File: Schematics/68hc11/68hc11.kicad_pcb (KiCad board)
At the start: 2 copper layers, 14 parts, among them J1 DB9_Female_MountingHoles, U1 MC68HC11A1CC-PLLC, U2 MC68B21, U3 74HC373, U4 74HC245, U6 27C64, U7 27C64, U8 HM62256BLP, U9 MAX232

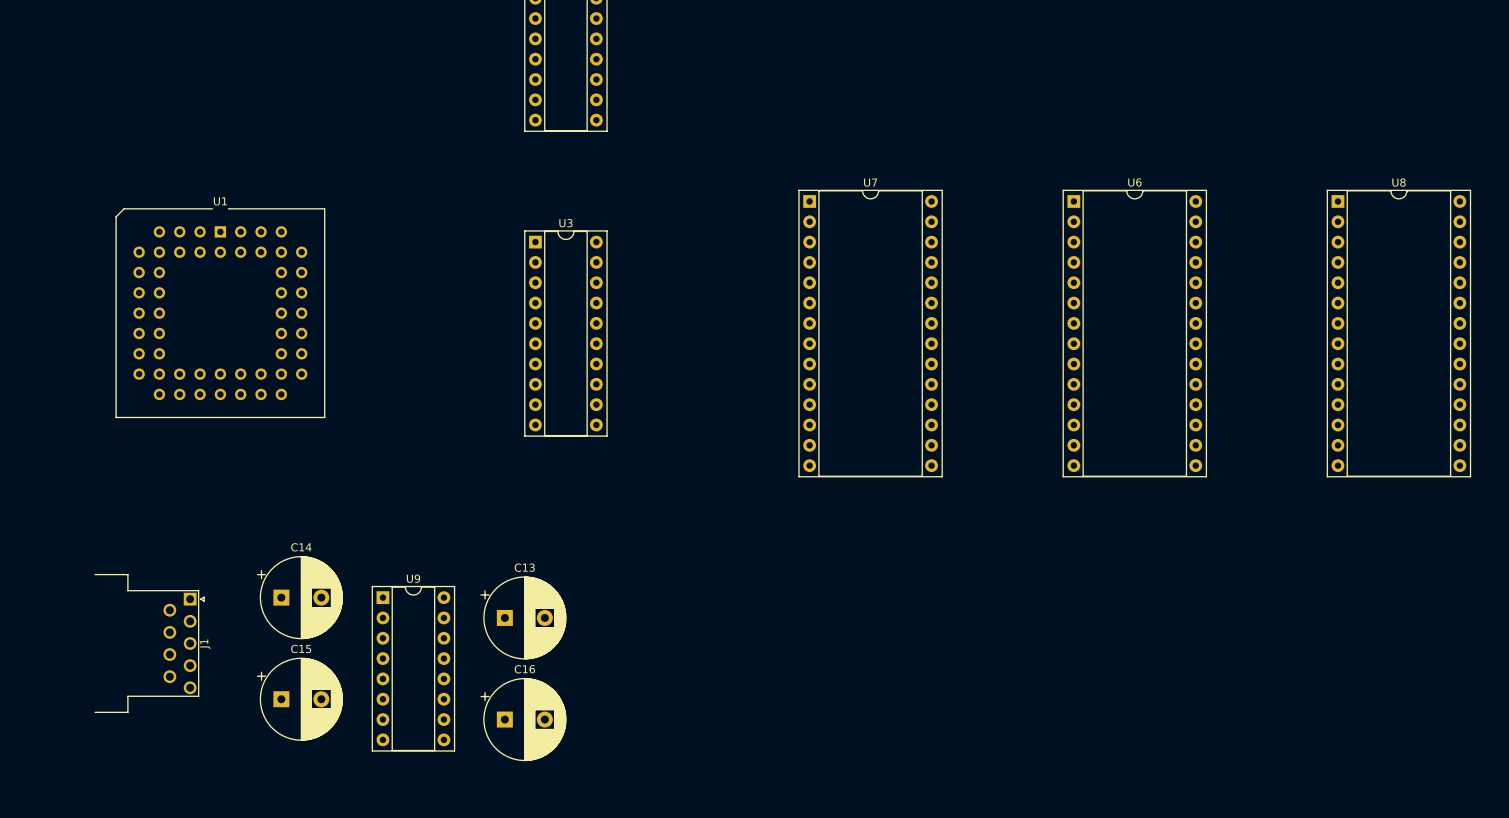
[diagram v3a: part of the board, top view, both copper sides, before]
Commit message: Added Crystal and some trace routing
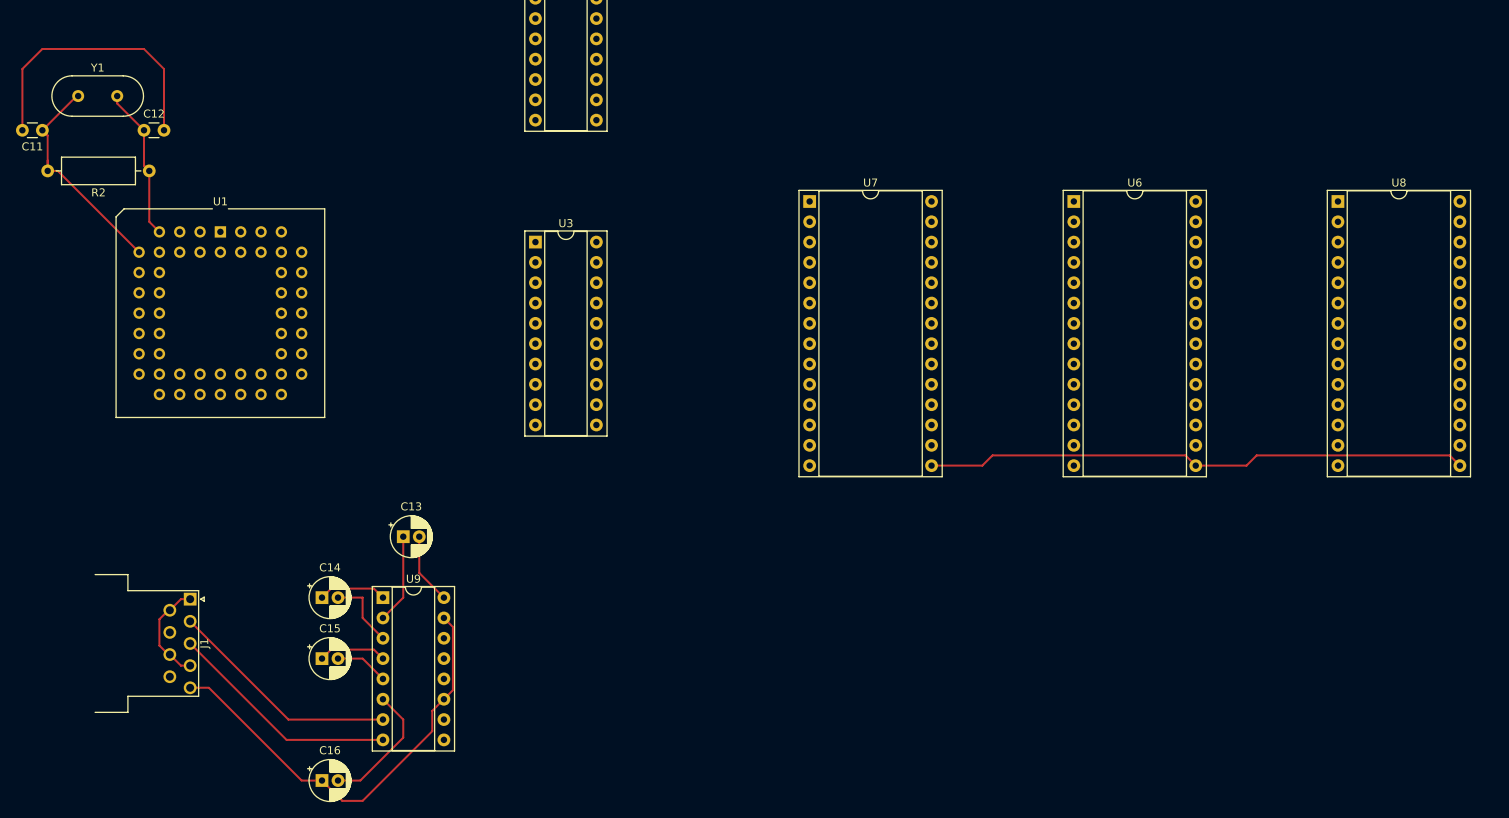
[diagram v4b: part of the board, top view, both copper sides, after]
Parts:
- added C11: 22pF, Capacitor_THT:C_Disc_D3.0mm_W1.6mm_P2.50mm, F.Cu at (20.9, 88.9)
- added C12: 22pF, Capacitor_THT:C_Disc_D3.0mm_W1.6mm_P2.50mm, F.Cu at (33.6, 88.9)
- added R2: 10 MO, Resistor_THT:R_Axial_DIN0309_L9.0mm_D3.2mm_P12.70mm_Horizontal, F.Cu at (34.3, 94.0)
- added Y1: 8.0 MHz, Crystal:Crystal_HC49-4H_Vertical, F.Cu at (25.4, 84.6)
- C13, C14, C15, C16: footprint Capacitor_THT:CP_Radial_D10.0mm_P5.00mm -> Capacitor_THT:CP_Radial_D5.0mm_P2.00mm
- RN1: value R_Network07_US -> 4.7 kO
- moved C16 24.1 mm to (55.9, 170.2)
- moved C13 16.3 mm to (66.0, 139.7)
- moved C15 7.18 mm to (55.9, 154.9)
- moved C14 5.08 mm to (55.9, 147.3)
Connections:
- net Net-(C13-Pad1) renamed /VS+
- net Net-(C14-Pad1) renamed /C1+
- net Net-(C14-Pad2) renamed /C1-
- net Net-(C15-Pad1) renamed /C2+
- net Net-(C15-Pad2) renamed /C2-
- net Net-(C16-Pad2) renamed /VS-
- net Net-(J1-Pad2) renamed /T2OUT
- net Net-(J1-Pad3) renamed /R2IN
- U1 pad 27: unconnected-(U1-Pad27) -> /PA7
- U1 pad 28: unconnected-(U1-Pad28) -> /PA6
- U1 pad 29: unconnected-(U1-Pad29) -> /PA5
- U1 pad 30: unconnected-(U1-Pad30) -> /PA4
- U1 pad 31: unconnected-(U1-Pad31) -> /PA3
- U1 pad 32: unconnected-(U1-Pad32) -> /PA2
- U1 pad 33: unconnected-(U1-Pad33) -> /PA1
- U1 pad 34: unconnected-(U1-Pad34) -> /PA0
- U1 pad 43: unconnected-(U1-Pad43) -> /PE0
- U1 pad 44: unconnected-(U1-Pad44) -> /PE4
- U1 pad 45: unconnected-(U1-Pad45) -> /PE1
- U1 pad 46: unconnected-(U1-Pad46) -> /PE5
- U1 pad 47: unconnected-(U1-Pad47) -> /PE2
- U1 pad 48: unconnected-(U1-Pad48) -> /PE6
- U1 pad 49: unconnected-(U1-Pad49) -> /PE3
- U1 pad 50: unconnected-(U1-Pad50) -> /PE7
- U1 pad 7: unconnected-(U1-Pad7) -> Net-(U1-Pad7)
- U1 pad 8: unconnected-(U1-Pad8) -> Net-(U1-Pad8)
- U2 pad 10: unconnected-(U2-Pad10) -> /PPB0
- U2 pad 11: unconnected-(U2-Pad11) -> /PPB1
- U2 pad 12: unconnected-(U2-Pad12) -> /PPB2
- U2 pad 13: unconnected-(U2-Pad13) -> /PPB3
- U2 pad 14: unconnected-(U2-Pad14) -> /PPB4
- U2 pad 15: unconnected-(U2-Pad15) -> /PPB5
- U2 pad 16: unconnected-(U2-Pad16) -> /PPB6
- U2 pad 17: unconnected-(U2-Pad17) -> /PPB7
- U2 pad 18: unconnected-(U2-Pad18) -> /CB1
- U2 pad 19: unconnected-(U2-Pad19) -> /CB2
- U2 pad 2: unconnected-(U2-Pad2) -> /PPA0
- U2 pad 3: unconnected-(U2-Pad3) -> /PPA1
- U2 pad 39: unconnected-(U2-Pad39) -> /CA2
- U2 pad 4: unconnected-(U2-Pad4) -> /PPA2
- U2 pad 40: unconnected-(U2-Pad40) -> /CA1
- U2 pad 5: unconnected-(U2-Pad5) -> /PPA3
- U2 pad 6: unconnected-(U2-Pad6) -> /PPA4
- U2 pad 7: unconnected-(U2-Pad7) -> /PPA5
- U2 pad 8: unconnected-(U2-Pad8) -> /PPA6
- U2 pad 9: unconnected-(U2-Pad9) -> /PPA7
- U4 pad 1: /R/W -> unconnected-(U4-Pad1)
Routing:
- net GND: track 0.00 -> 90.5 mm
- net /D3: track 0.00 -> 68.2 mm
- net /T2OUT: track 0.00 -> 29.2 mm
- net /R2IN: track 0.00 -> 29.1 mm
- net Net-(U1-Pad8): track 0.00 -> 28.5 mm
- net Net-(U1-Pad7): track 0.00 -> 19.2 mm
- net /VS-: track 0.00 -> 16.2 mm
- net Net-(J1-Pad1): track 0.00 -> 12.7 mm
- net /VS+: track 0.00 -> 11.2 mm
- net /C1-: track 0.00 -> 9.21 mm
- net VCC: track 0.00 -> 8.90 mm
- net /C2+: track 0.00 -> 8.55 mm
- net /C1+: track 0.00 -> 8.55 mm
- net /C2-: track 0.00 -> 6.67 mm

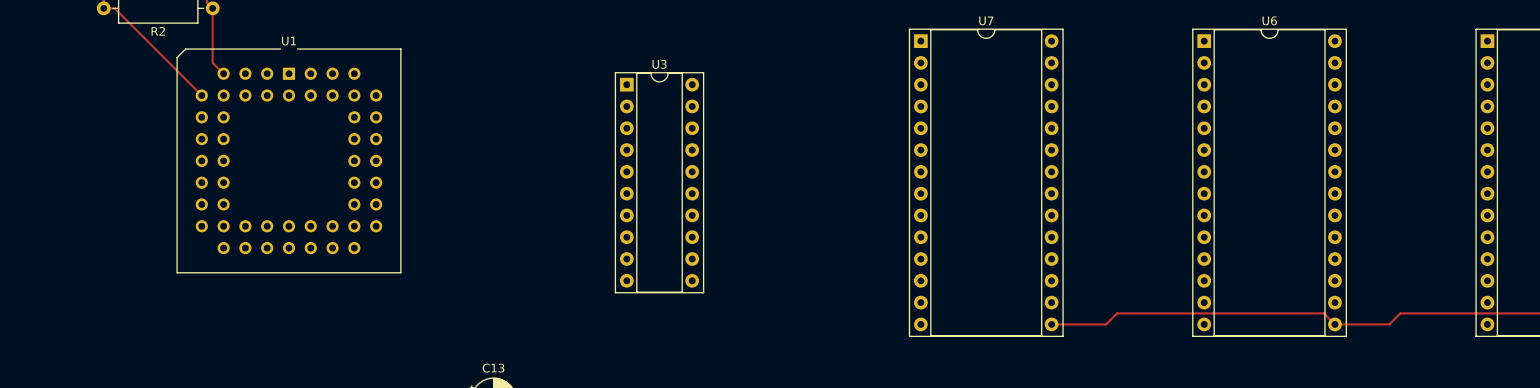
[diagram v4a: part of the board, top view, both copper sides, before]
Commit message: Added low power reset and cleaned up busses
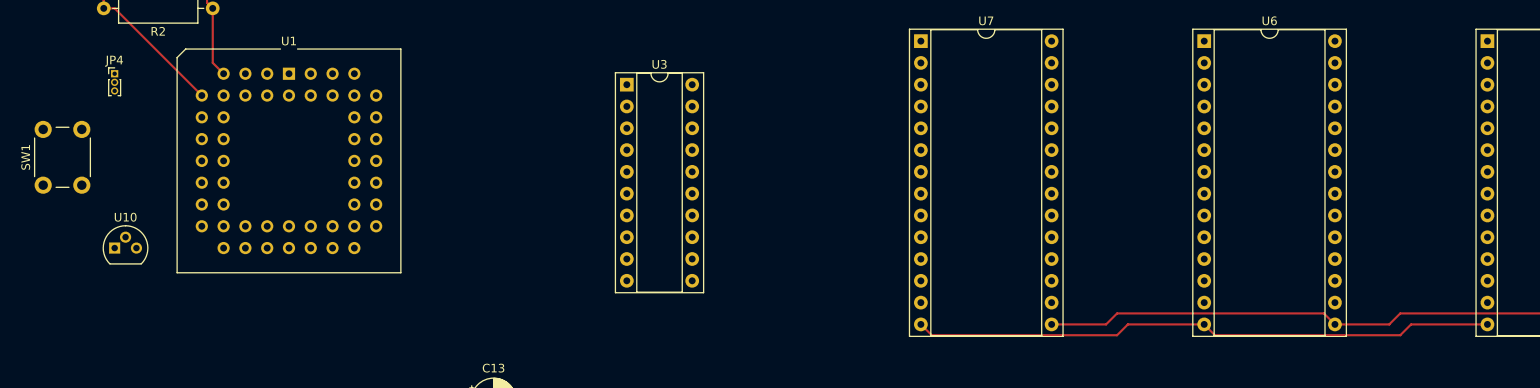
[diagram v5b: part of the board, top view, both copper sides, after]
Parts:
- added JP4: BootSel, Connector_PinHeader_1.00mm:PinHeader_1x03_P1.00mm_Vertical, F.Cu at (22.9, 101.6)
- added SW1: Reset, Button_Switch_THT:SW_PUSH_6mm, F.Cu at (14.5, 114.6)
- added U10: MCP100-270D, Package_TO_SOT_THT:TO-92, F.Cu at (22.9, 121.9)
- J1: value DB9_Female_MountingHoles -> DB9_Female
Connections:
- net /RXD renamed /RxD
- net /TXD renamed /TxD
- net Net-(J1-Pad1) renamed /CTS
- net Net-(RN1-Pad7) renamed /MODB
- net Net-(RN1-Pad8) renamed /MODA
- net Net-(U1-Pad7) renamed /EXTAL
- net Net-(U1-Pad8) renamed /XTAL
- RN1 pad 4: unconnected-(RN1-Pad4) -> /*RESET
- U1 pad 17: unconnected-(U1-Pad17) -> /*RESET
- U1 pad 4: /AS -> GND
- U1 pad 5: unconnected-(U1-Pad5) -> /E
- U1 pad 52: unconnected-(U1-Pad52) -> /VRH
- U1 pad 6: /R/W -> /R/*W
- U2 pad 21: unconnected-(U2-Pad21) -> /R/*W
- U2 pad 22: unconnected-(U2-Pad22) -> VCC
- U2 pad 23: unconnected-(U2-Pad23) -> /*PIA1
- U2 pad 24: unconnected-(U2-Pad24) -> VCC
- U2 pad 25: unconnected-(U2-Pad25) -> /E
- U2 pad 34: unconnected-(U2-Pad34) -> /*RESET
- U2 pad 35: unconnected-(U2-Pad35) -> /A1
- U2 pad 36: unconnected-(U2-Pad36) -> /A0
- U3 pad 11: /AS -> GND
- U4 pad 1: unconnected-(U4-Pad1) -> /R/*W
- U4 pad 19: /AS -> GND
- U6 pad 1: +5V -> VCC
- U6 pad 20: unconnected-(U6-Pad20) -> GND
- U6 pad 22: GND -> /*BOOT
- U6 pad 27: +5V -> VCC
- U7 pad 1: +5V -> VCC
- U7 pad 20: unconnected-(U7-Pad20) -> GND
- U7 pad 22: GND -> /*SPARE
- U7 pad 27: +5V -> VCC
- U8 pad 20: unconnected-(U8-Pad20) -> /*RAM
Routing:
- net GND: track 90.5 -> 158.6 mm

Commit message: Traced Data Bus between ROM, RAM and PCIA
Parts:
- C15: value 19 uF -> 10 uF
- moved C16 27.8 mm to (78.7, 154.4), turned to 90 degrees
- moved C13 14.8 mm to (78.7, 147.3), turned to 90 degrees
- moved C14 2.54 mm to (58.4, 147.3), turned to -90 degrees
- moved C15 2.54 mm to (58.4, 154.9), turned to -90 degrees
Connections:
- net VCC renamed +5V
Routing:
- net /D2: track 0.00 -> 129.0 mm, vias 0 -> 1
- net /D1: track 0.00 -> 125.9 mm, vias 0 -> 2
- net /D0: track 0.00 -> 125.8 mm, vias 0 -> 1
- net GND: track 158.6 -> 36.9 mm
- net /D4: track 0.00 -> 112.4 mm, vias 0 -> 2
- net /D5: track 0.00 -> 104.6 mm, vias 0 -> 1
- net /D6: track 0.00 -> 101.2 mm, vias 0 -> 1
- net /D7: track 0.00 -> 99.6 mm, vias 0 -> 3
- net /A0: track 0.00 -> 68.2 mm
- net /D3: track 68.2 -> 117.4 mm, vias 0 -> 1
- net /VS-: track 16.2 -> 30.7 mm
- net /VS+: track 11.2 -> 17.2 mm
- net /C2+: track 8.55 -> 5.08 mm
- net /C1+: track 8.55 -> 5.08 mm
- net /C1-: track 9.21 -> 6.36 mm
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- added copper zone on B.Cu, net GND

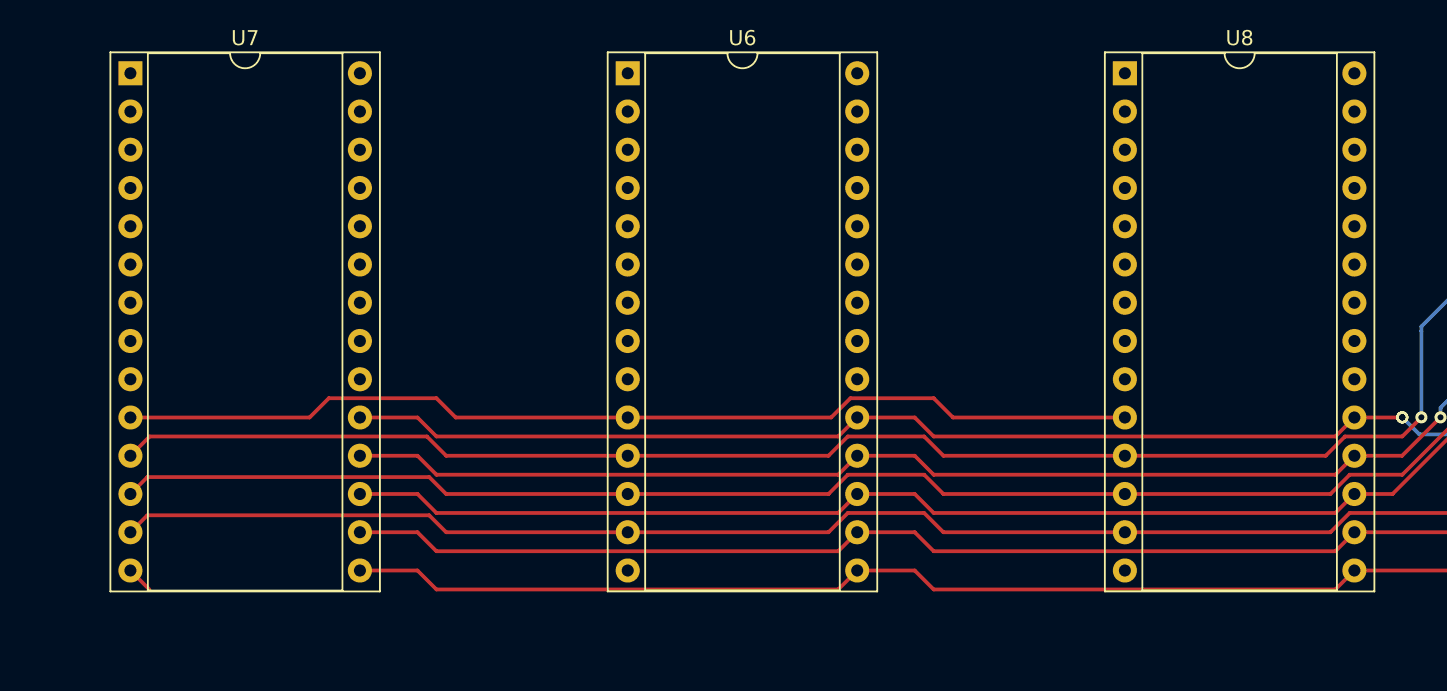
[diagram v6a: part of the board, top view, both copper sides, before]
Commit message: Traced out some more of the address bus
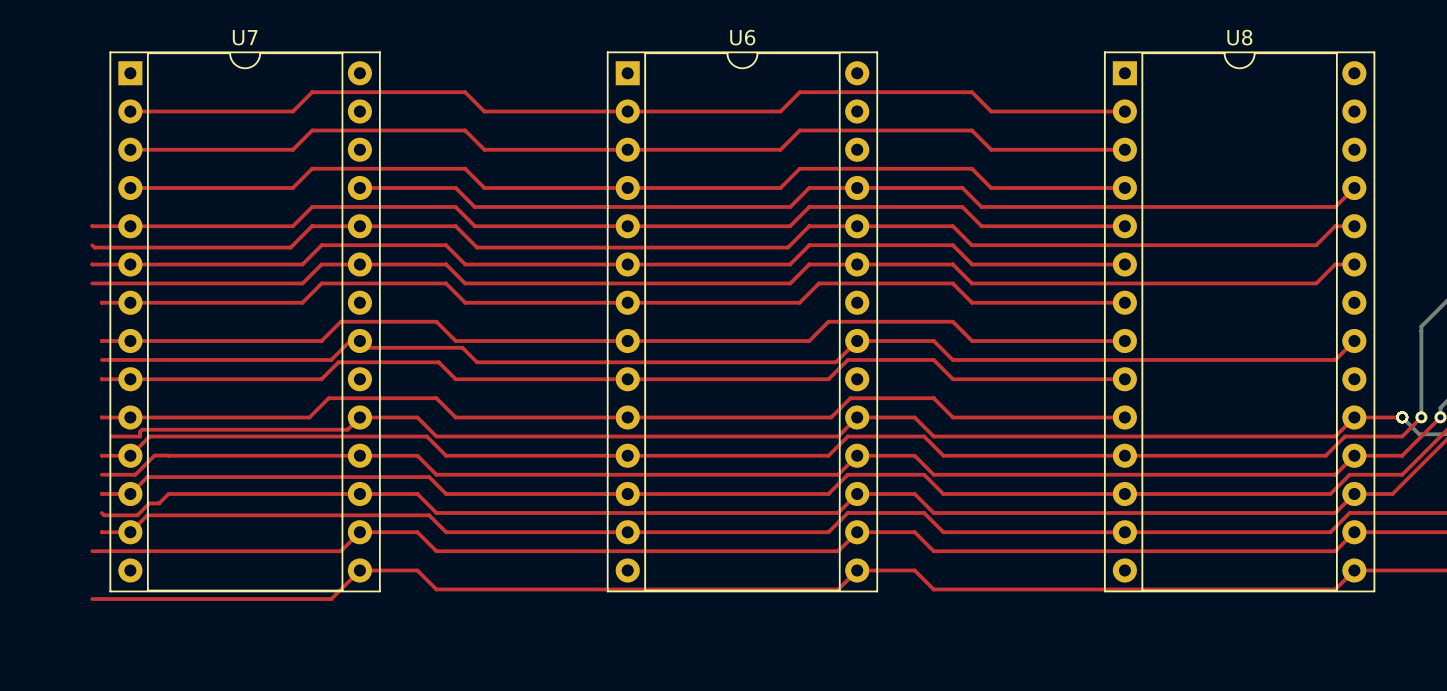
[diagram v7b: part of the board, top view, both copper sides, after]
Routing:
- net /A9: track 0.00 -> 86.7 mm
- net /A11: track 0.00 -> 86.4 mm
- net /A10: track 0.00 -> 85.9 mm
- net /A4: track 0.00 -> 70.7 mm
- net /A5: track 0.00 -> 70.7 mm
- net /A3: track 0.00 -> 70.1 mm
- net /A2: track 0.00 -> 70.1 mm
- net /A1: track 0.00 -> 69.9 mm
- net /A7: track 0.00 -> 68.2 mm
- net /A6: track 0.00 -> 68.2 mm
- net /A12: track 0.00 -> 68.2 mm
- net /A8: track 0.00 -> 68.1 mm
- net /D3: track 117.4 -> 136.0 mm
- net /D4: track 112.4 -> 130.7 mm
- net /D5: track 104.6 -> 122.4 mm
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
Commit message: Added Screw Terminals for IO Ports
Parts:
- added J2: Screw_Terminal_01x10, TerminalBlock_4Ucon:TerminalBlock_4Ucon_1x10_P3.50mm_Horizontal, F.Cu at (241.4, 118.0)
- added J3: Screw_Terminal_01x10, TerminalBlock_4Ucon:TerminalBlock_4Ucon_1x10_P3.50mm_Horizontal, F.Cu at (243.0, 158.0)
- added J4: Screw_Terminal_01x10, TerminalBlock_4Ucon:TerminalBlock_4Ucon_1x10_P3.50mm_Horizontal, F.Cu at (240.1, 35.2)
- added J5: Screw_Terminal_01x10, TerminalBlock_4Ucon:TerminalBlock_4Ucon_1x10_P3.50mm_Horizontal, F.Cu at (240.9, 77.4)
- C15: value 10 uF -> 19 uF
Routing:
- net /D3: track 136.0 -> 224.1 mm, vias 1 -> 2
- net /D2: track 130.9 -> 217.0 mm, vias 1 -> 2
- net /D1: track 127.8 -> 213.5 mm, vias 2 -> 3
- net /D0: track 127.7 -> 213.1 mm, vias 1 -> 2
- net /D4: track 130.7 -> 213.3 mm, vias 2 -> 3
- net /D5: track 122.4 -> 200.2 mm, vias 1 -> 2
- net /A0: track 70.1 -> 146.4 mm
- net /D6: track 118.9 -> 191.8 mm, vias 1 -> 2
- net /A1: track 69.9 -> 139.3 mm
- net /D7: track 116.8 -> 186.0 mm, vias 3 -> 4
- net /A2: track 70.1 -> 134.7 mm
- net /A3: track 70.1 -> 126.8 mm
- net /A4: track 70.7 -> 102.6 mm
- net /A5: track 70.7 -> 100.5 mm
- net /A6: track 68.2 -> 98.0 mm
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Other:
- board outline added: 268.6 x 177.2 mm
